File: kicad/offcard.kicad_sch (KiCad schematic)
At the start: 26 parts, among them IC1 NAU7802KGI, J10 lower fan, J4 heater, J5 5kg load cell, J6 LCD, J7 upper fan, J8 motor, Q2 SSM3K127TU, Q3 T1210-800G

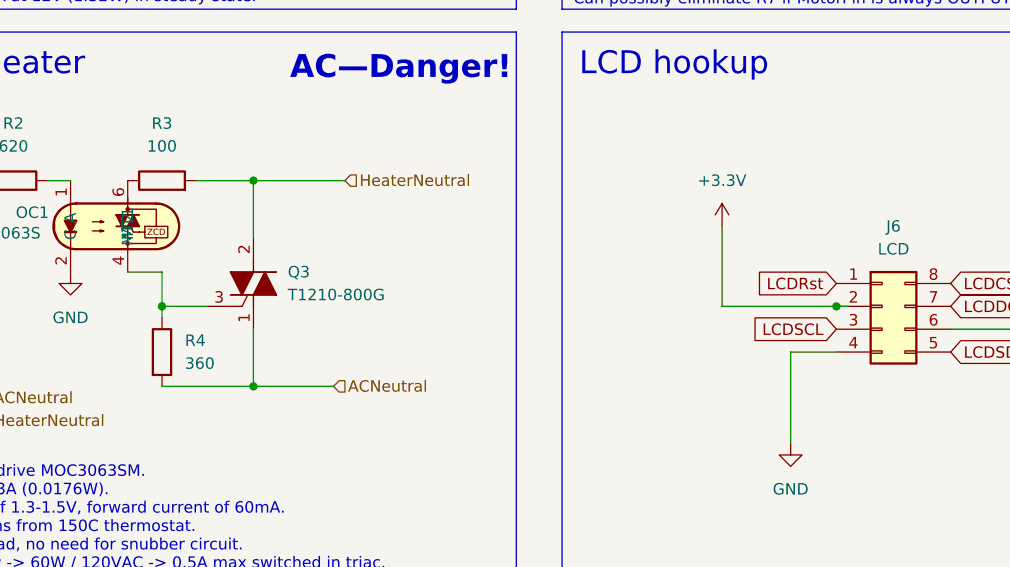
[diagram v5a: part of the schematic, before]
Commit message: update footprint for tps62132
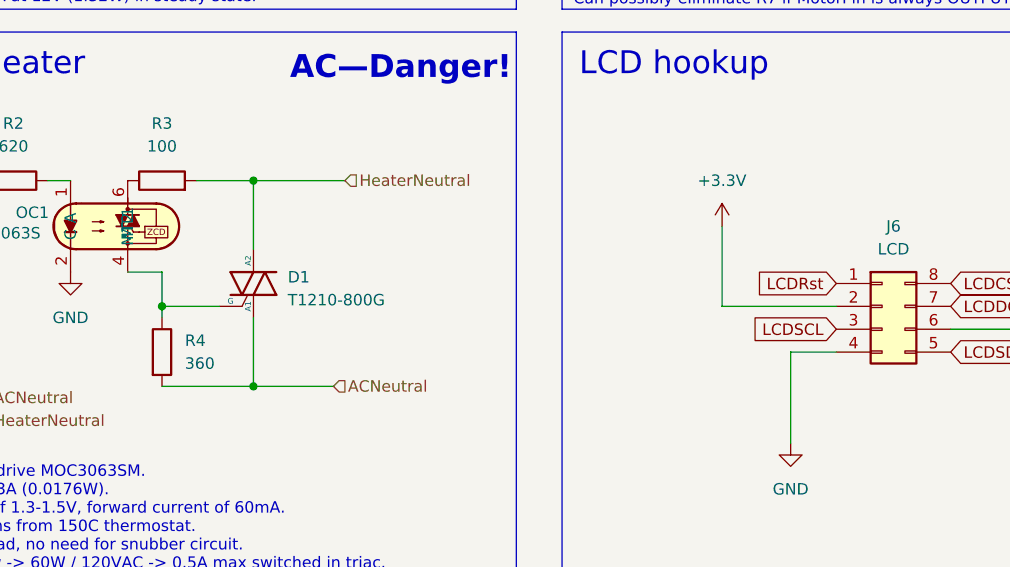
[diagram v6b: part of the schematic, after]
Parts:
- removed Q3: T1210-800G, dank:T1210-800G-TR, symbol PCM_Triac_AKL:T1210-800G
- added D1: T1210-800G, dank:T1210-800G-TR, symbol Device:Q_Triac
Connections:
- net ACNeutral: now also D1.A1
- net HeaterNeutral: now also D1.A2
- net at OC1.4 (MT1), R4.1: now also D1.G
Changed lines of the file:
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@@
 	(title_block
 		(title "dankdryer")
-		(date "2025-02-21")
-		(rev "1.7.3")
+		(date "2025-02-26")
+		(rev "1.8.0")
 		(company "dirty south supercomputing")
 		(comment 1 "nick black")
@@
 	)
 	(junction
-		(at 127 134.62)
-		(diameter 0)
-		(color 0 0 0 0)
-	)
-	(junction
 		(at 62.23 120.65)
 		(diameter 0)
@@
 	(wire
 		(pts
-			(xy 62.23 137.16) (xy 62.23 143.51)
+			(xy 62.23 135.89) (xy 62.23 143.51)
 		)
 		(stroke
@@
 	(wire
 		(pts
-			(xy 127 134.62) (xy 128.27 134.62)
-		)
-		(stroke
-			(width 0)
-			(type default)
-		)
-	)
-	(wire
-		(pts
 			(xy 144.78 39.37) (xy 144.78 41.91)
 		)
@@
 	(wire
 		(pts
-			(xy 62.23 120.65) (xy 62.23 127)
+			(xy 62.23 120.65) (xy 62.23 128.27)
 		)
 		(stroke
@@
 	(wire
 		(pts
-			(xy 52.07 134.62) (xy 57.15 134.62)
+			(xy 52.07 134.62) (xy 58.42 134.62)
 		)
 		(stroke
@@
 	)
 	(symbol
+		(lib_id "Device:Q_Triac")
+		(at 62.23 132.08 0)
+		(unit 1)
+		(exclude_from_sim no)
+		(in_bom yes)
+		(on_board yes)
+		(dnp no)
+		(fields_autoplaced yes)
+		(property "Reference" "D1"
+			(at 66.04 131.3814 0)
+			(effects
+				(font
+					(size 1.27 1.27)
+				)
+				(justify left)
+			)
+		)
+		(property "Value" "T1210-800G"
+			(at 66.04 133.9214 0)
+			(effects
+				(font
+					(size 1.27 1.27)
+				)
+				(justify left)
+			)
+		)
+		(property "Footprint" "dank:T1210-800G-TR"
+			(at 64.135 131.445 90)
+			(effects
+				(font
+					(size 1.27 1.27)
+				)
+				(hide yes)
+			)
+		)
+		(property "Datasheet" "~"
+			(at 62.23 132.08 90)
+			(effects
+				(font
+					(size 1.27 1.27)
+				)
+				(hide yes)
+			)
+		)
+		(property "Description" "Triode for alternating current, generic/no defined pinout"
+			(at 62.23 132.08 0)
+			(effects
+				(font
+					(size 1.27 1.27)
+				)
+				(hide yes)
+			)
+		)
+		(pin "A1"
+		)
+		(pin "G"
+		)
+		(pin "A2"
+		)
+		(instances
+			(project ""
+				(path "/0e28ce9c-097a-4614-9b8c-9333a7b96611/2a0e6a8d-8569-4b27-a15d-bed47a66289a"
+					(reference "D1")
+					(unit 1)
+				)
+			)
+		)
+	)
+	(symbol
 		(lib_id "Device:C")
 		(at 203.2 52.07 90)
@@
 					(unit 1)
 				)
-			)
-		)
-	)
-	(symbol
-		(lib_id "PCM_Triac_AKL:T1210-800G")
-		(at 62.23 132.08 0)
-		(unit 1)
-		(exclude_from_sim no)
-		(in_bom yes)
-		(on_board yes)
-		(dnp no)
-		(fields_autoplaced yes)
-		(property "Reference" "Q3"
-			(at 66.04 130.8099 0)
-			(effects
-				(font
-					(size 1.27 1.27)
-				)
-				(justify left)
-			)
-		)
-		(property "Value" "T1210-800G"
-			(at 66.04 133.3499 0)
-			(effects
-				(font
-					(size 1.27 1.27)
-				)
-				(justify left)
-			)
-		)
-		(property "Footprint" "dank:T1210-800G-TR"
-			(at 62.23 132.08 0)
-			(effects
-				(font
-					(size 1.27 1.27)
-				)
-				(hide yes)
-			)
-		)
-		(property "Datasheet" "https://www.tme.eu/Document/76a9cc135e61671358387fc748b5f228/BTA12_BTB12_T12xx.pdf"
-			(at 62.23 132.08 0)
-			(effects
-				(font
-					(size 1.27 1.27)
-				)
-				(hide yes)
-			)
-		)
-		(property "Description" "TO-263 Triac, 800V, 12A, Alternate KiCAD Library"
-			(at 62.23 132.08 0)
-			(effects
-				(font
-					(size 1.27 1.27)
-				)
-				(hide yes)
-			)
-		)
-		(pin "3"
-		)
-		(pin "1"
-		)
-		(pin "2"
-		)
-		(instances
-			(project ""
-				(path "/0e28ce9c-097a-4614-9b8c-9333a7b96611/2a0e6a8d-8569-4b27-a15d-bed47a66289a"
-					(reference "Q3")
-					(unit 1)
-				)

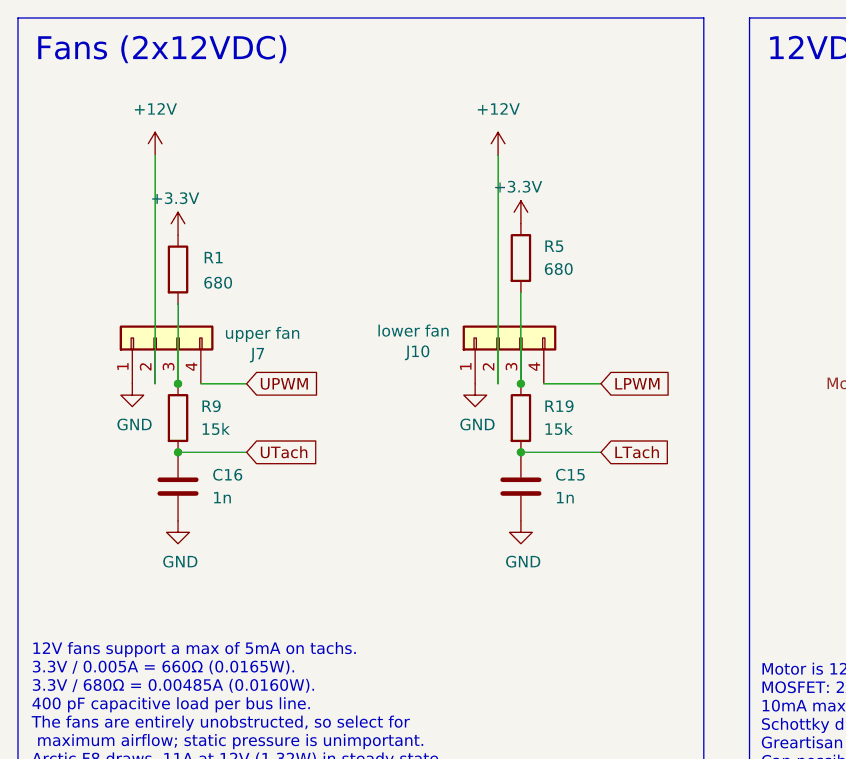
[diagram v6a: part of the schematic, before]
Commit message: [miniboard] throughholes need [5, -5] separation #99
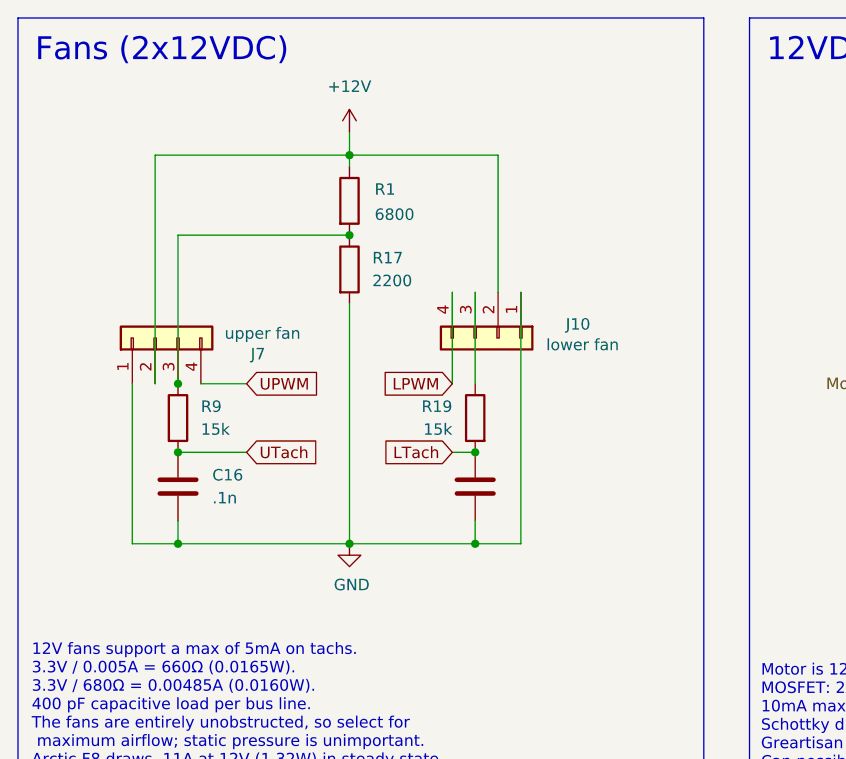
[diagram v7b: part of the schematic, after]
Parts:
- removed R5: 680, Resistor_SMD:R_1206_3216Metric_Pad1.30x1.75mm_HandSolder, symbol Device:R
- added R17: 2200, Resistor_SMD:R_0805_2012Metric_Pad1.20x1.40mm_HandSolder, symbol Device:R
- C15, C16: value 1n -> .1n; footprint Capacitor_SMD:C_1206_3216Metric_Pad1.33x1.80mm_HandSolder -> Capacitor_SMD:C_0805_2012Metric_Pad1.18x1.45mm_HandSolder
- R1: value 680 -> 6800
- R19, R2, R3, R4, R9: footprint Resistor_SMD:R_1206_3216Metric_Pad1.30x1.75mm_HandSolder -> Resistor_SMD:R_0805_2012Metric_Pad1.20x1.40mm_HandSolder
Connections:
- net +12V: now also R1.1
- net +3.3V: no longer R1.1
- net GND: now also R17.2
- net at J7.3 (Pin_3), R1.2, R9.1: now also R17.1
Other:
- moved on the sheet: J10, R1, R19

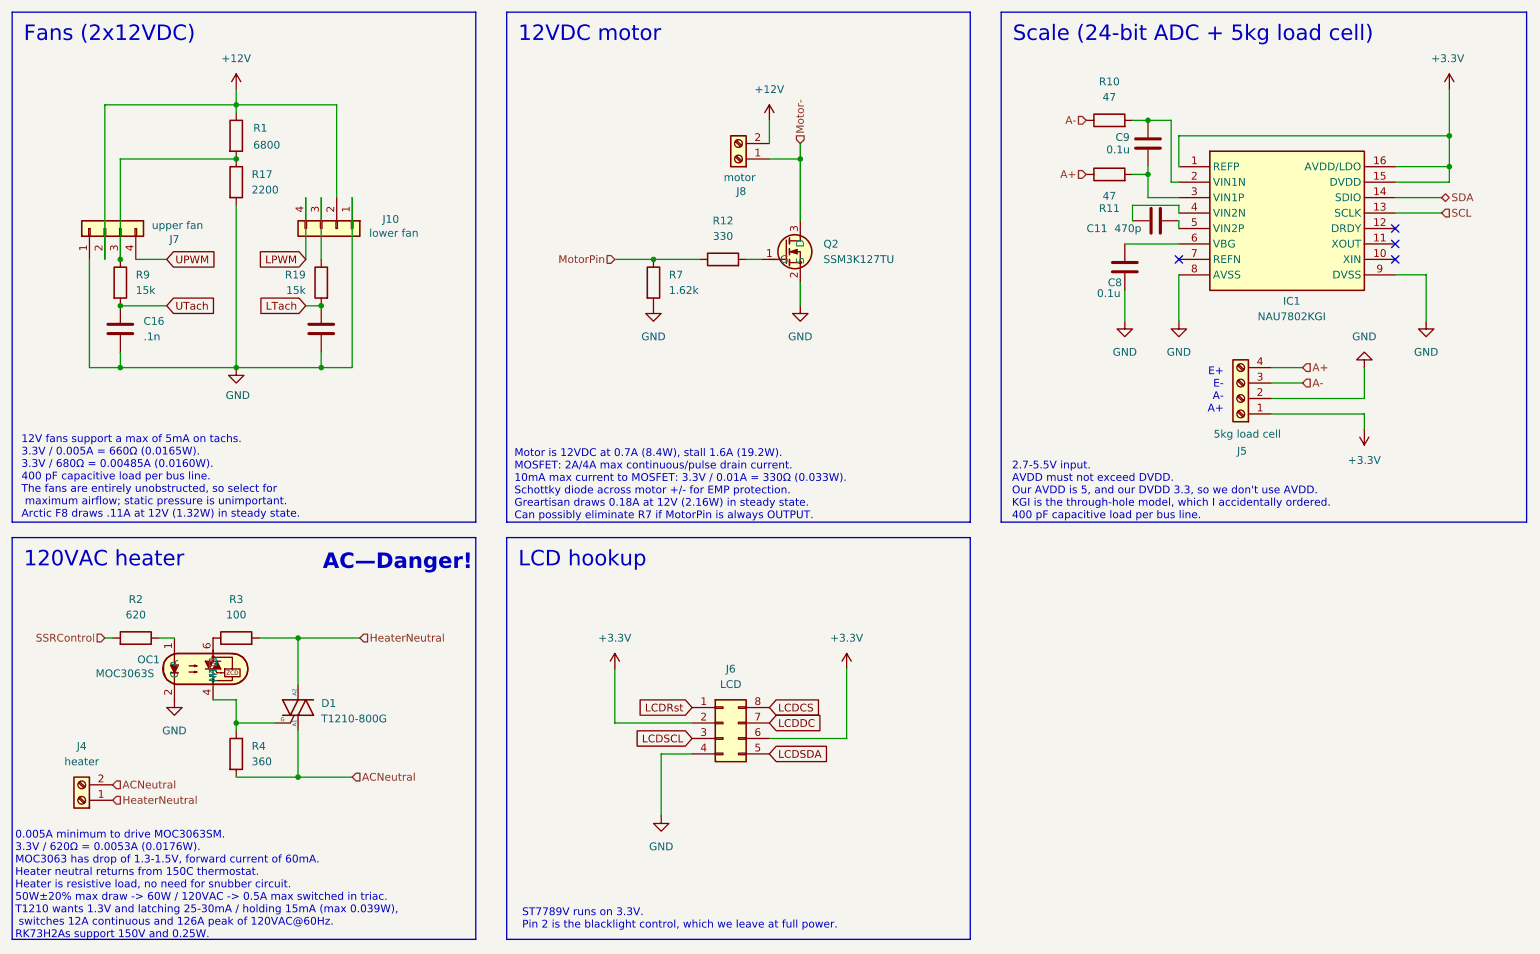
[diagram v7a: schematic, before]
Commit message: [pcb] don't run trace between connectors #97
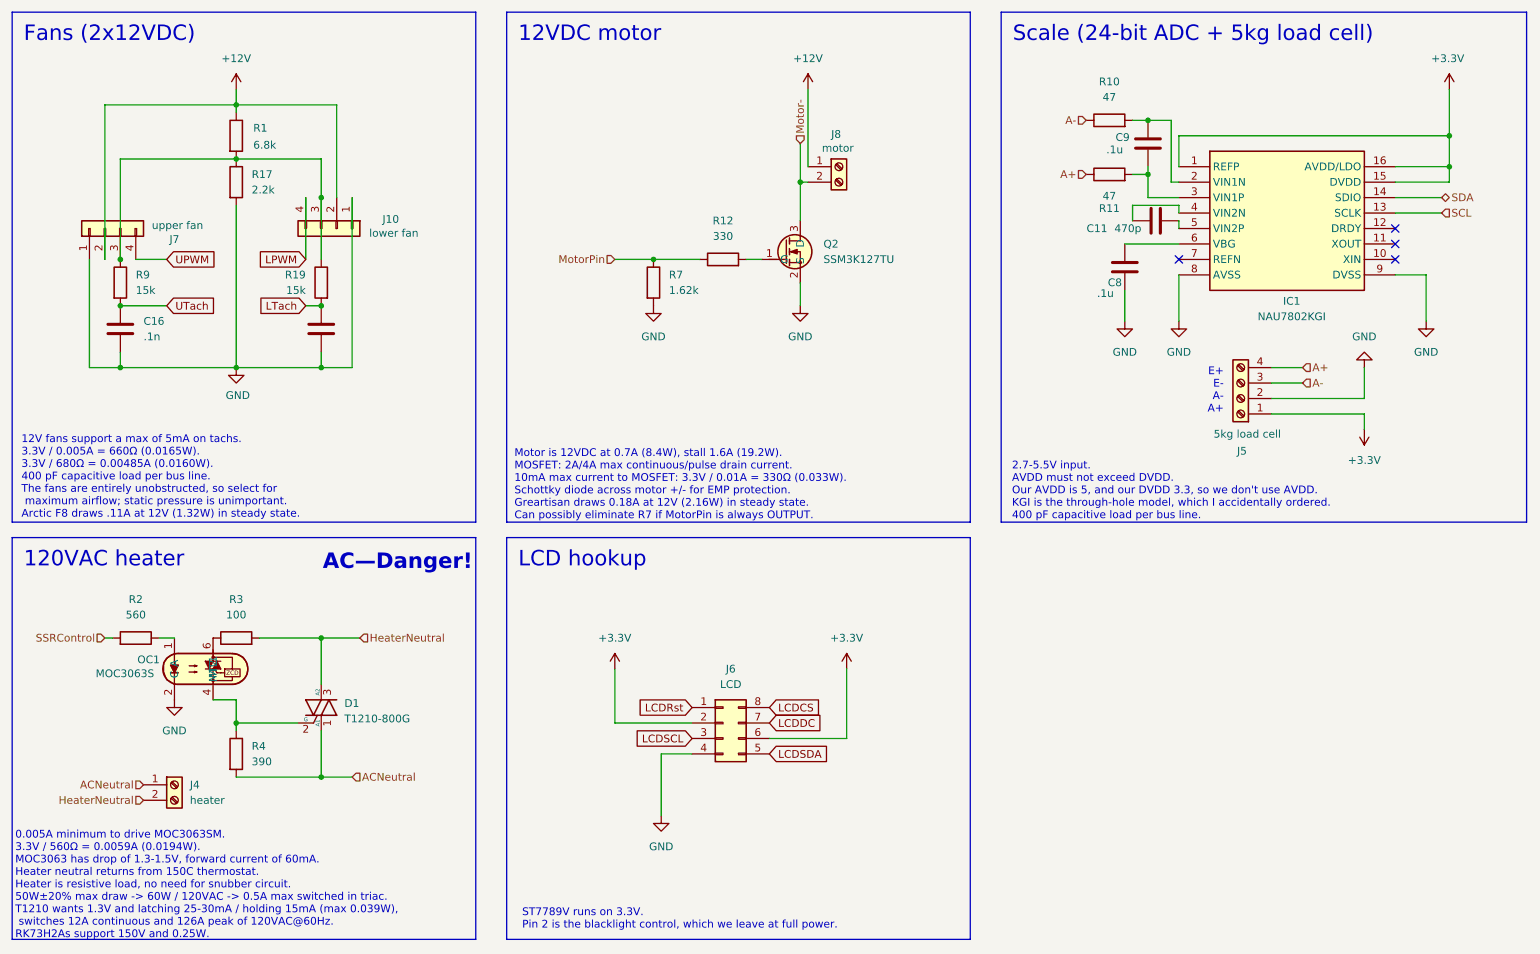
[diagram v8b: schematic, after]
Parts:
- removed D1: T1210-800G, dank:T1210-800G-TR, symbol Device:Q_Triac
- added D1: T1210-800G, dank:T1210-800G-TR, symbol Triac_Thyristor:Generic_Triac_A1GA2
- C8, C9: value 0.1u -> .1u; footprint Capacitor_SMD:C_1206_3216Metric_Pad1.33x1.80mm_HandSolder -> Capacitor_SMD:C_0805_2012Metric_Pad1.18x1.45mm_HandSolder
- R1: value 6800 -> 6.8k; footprint Resistor_SMD:R_1206_3216Metric_Pad1.30x1.75mm_HandSolder -> Resistor_SMD:R_0805_2012Metric_Pad1.20x1.40mm_HandSolder
- R10, R11, R12, R7: footprint Resistor_SMD:R_1206_3216Metric_Pad1.30x1.75mm_HandSolder -> Resistor_SMD:R_0805_2012Metric_Pad1.20x1.40mm_HandSolder
- R17: value 2200 -> 2.2k
- R2: value 620 -> 560
- R4: value 360 -> 390
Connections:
- net +12V: now also J8.1 (Pin_1); no longer J8.2 (Pin_2)
- net ACNeutral: now also J4.1 (Pin_1), D1.1 (A1); no longer J4.2 (Pin_2)
- net HeaterNeutral: now also J4.2 (Pin_2), D1.3 (A2); no longer J4.1 (Pin_1)
- net Motor-: now also J8.2 (Pin_2); no longer J8.1 (Pin_1)
- net at J7.3 (Pin_3), R1.2, R17.1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: now also J10.3 (Pin_3), R19.1
- net at OC1.4 (MT1), R4.1: now also D1.2 (G)
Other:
- note added: "0.005A minimum to drive MOC3063SM. 3.3V / 560Ω = 0.0059A (0.0194W). MOC3063 has drop of 1.3-1.5V, forward current of 60mA. Heater neutral returns from 150C thermostat. Heater is resistive load, no need for snubber circuit. 50W±20% max draw -> 60W / 120VAC -> 0.5A max switched in triac. T1210 wants 1.3V and latching 25-30mA / holding 15mA (max 0.039W), switches 12A continuous and 126A peak of 120V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"
- note removed: "0.005A minimum to drive MOC3063SM. 3.3V / 620Ω = 0.0053A (0.0176W). MOC3063 has drop of 1.3-1.5V, forward current of 60mA. Heater neutral returns from 150C thermostat. Heater is resistive load, no need for snubber circuit. 50W±20% max draw -> 60W / 120VAC -> 0.5A max switched in triac. T1210 wants 1.3V and latching 25-30mA / holding 15mA (max 0.039W), switches 12A continuous and 126A peak of 120V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"
- moved on the sheet: J4, J8
